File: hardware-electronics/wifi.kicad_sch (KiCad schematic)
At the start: 0 parts

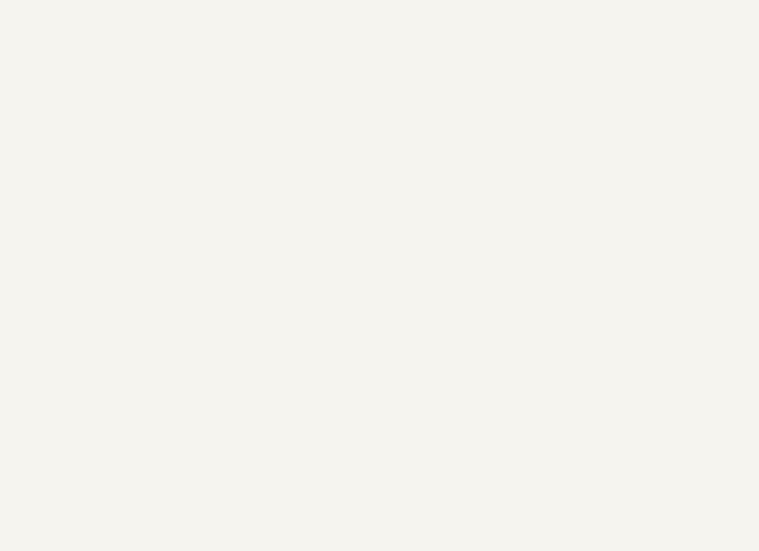
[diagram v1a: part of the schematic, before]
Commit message: [#9] SCH wifi add RTL8188FTV-VC-CG
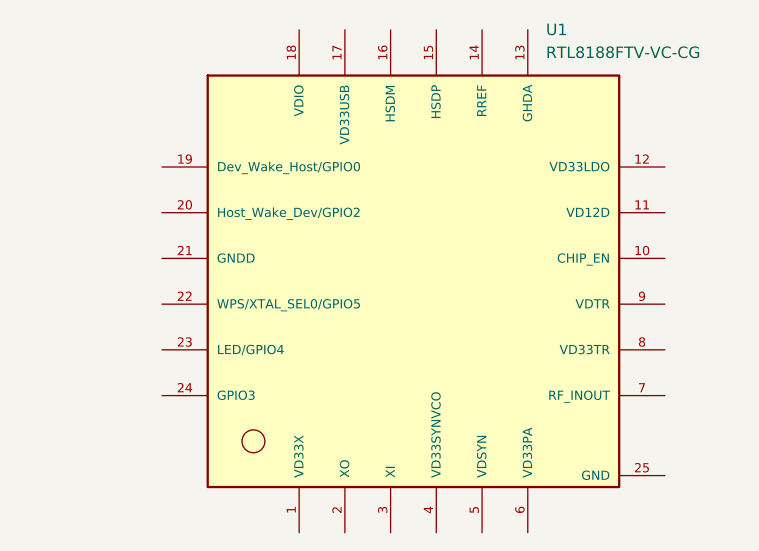
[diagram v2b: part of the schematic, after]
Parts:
- added U1: RTL8188FTV-VC-CG, RTL8188FTV-VC-CG, symbol M2SmartHomeSymbols:RTL8188FTV-VC-CG
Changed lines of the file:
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@@
+		)
+	)
+	(symbol
+		(lib_id "M2SmartHomeSymbols:RTL8188FTV-VC-CG")
+		(at 144.78 96.52 0)
+		(unit 1)
+		(exclude_from_sim no)
+		(in_bom yes)
+		(on_board yes)
+		(dnp no)
+		(fields_autoplaced yes)
+		(property "Reference" "U1"
+			(at 159.4994 68.58 0)
+			(effects
+				(font
+					(size 1.27 1.27)
+				)
+				(justify left)
+			)
+		)
+		(property "Value" "RTL8188FTV-VC-CG"
+			(at 159.4994 71.12 0)
+			(effects
+				(font
+					(size 1.27 1.27)
+				)
+				(justify left)
+			)
+		)
+		(property "Footprint" "RTL8188FTV-VC-CG"
+			(at 144.78 96.52 0)
+			(effects
+				(font
+					(size 1.27 1.27)
+				)
+				(justify bottom)
+				(hide yes)
+			)
+		)
+		(property "Datasheet" ""
+			(at 144.78 96.52 0)
+			(effects
+				(font
+					(size 1.27 1.27)
+				)
+				(hide yes)
+			)
+		)
+		(property "Description" ""
+			(at 144.78 96.52 0)
+			(effects
+				(font
+					(size 1.27 1.27)
+				)
+				(hide yes)
+			)
+		)
+		(property "MF" "Realtek"
+			(at 144.78 96.52 0)
+			(effects
+				(font
+					(size 1.27 1.27)
+				)
+				(justify bottom)
+				(hide yes)
+			)
+		)
+		(property "Description_1" ""
+			(at 144.78 96.52 0)
+			(effects
+				(font
+					(size 1.27 1.27)
+				)
+				(justify bottom)
+				(hide yes)
+			)
+		)
+		(property "Package" "QFN-24 Silicon Labs"
+			(at 144.78 96.52 0)
+			(effects
+				(font
+					(size 1.27 1.27)
+				)
+				(justify bottom)
+				(hide yes)
+			)
+		)
+		(property "Price" "None"
+			(at 144.78 96.52 0)
+			(effects
+				(font
+					(size 1.27 1.27)
+				)
+				(justify bottom)
+				(hide yes)
+			)
+		)
+		(property "Check_prices" ""
+			(at 144.78 96.52 0)
+			(effects
+				(font
+					(size 1.27 1.27)
+				)
+				(justify bottom)
+				(hide yes)
+			)
+		)
+		(property "PART_REV" "1.1"
+			(at 144.78 96.52 0)
+			(effects
+				(font
+					(size 1.27 1.27)
+				)
+				(justify bottom)
+				(hide yes)
+			)
+		)
+		(property "STANDARD" ""
+			(at 144.78 96.52 0)
+			(effects
+				(font
+					(size 1.27 1.27)
+				)
+				(justify bottom)
+				(hide yes)
+			)
+		)
+		(property "SnapEDA_Link" ""
+			(at 144.78 96.52 0)
+			(effects
+				(font
+					(size 1.27 1.27)
+				)
+				(justify bottom)
+				(hide yes)
+			)
+		)
+		(property "MP" "RTL8188FTV-VC-CG"
+			(at 144.78 96.52 0)
+			(effects
+				(font
+					(size 1.27 1.27)
+				)
+				(justify bottom)
+				(hide yes)
+			)
+		)
+		(property "Availability" "In Stock"
+			(at 144.78 96.52 0)
+			(effects
+				(font
+					(size 1.27 1.27)
+				)
+				(justify bottom)
+				(hide yes)
+			)
+		)
+		(property "MANUFACTURER" "Realtek"
+			(at 144.78 96.52 0)
+			(effects
+				(font
+					(size 1.27 1.27)
+				)
+				(justify bottom)
+				(hide yes)
+			)
+		)
+		(pin "18"
+		)
+		(pin "17"
+		)
+		(pin "16"
+		)
+		(pin "21"
+		)
+		(pin "19"
+		)
+		(pin "20"
+		)
+		(pin "2"
+		)
+		(pin "3"
+		)
+		(pin "25"
+		)
+		(pin "14"
+		)
+		(pin "13"
+		)
+		(pin "12"
+		)
+		(pin "9"
+		)
+		(pin "11"
+		)
+		(pin "24"
+		)
+		(pin "23"
+		)
+		(pin "10"
+		)
+		(pin "1"
+		)
+		(pin "4"
+		)
+		(pin "15"
+		)
+		(pin "22"
+		)
+		(pin "6"
+		)
+		(pin "5"
+		)
+		(pin "8"
+		)
+		(pin "7"
+		)
+		(instances
+			(project "M2SmartHome"
+				(path "/da663dec-9e91-4003-a791-431d460ad63c/7a341d5c-2113-408f-a1b4-1e4771333f4d"
+					(reference "U1")
+					(unit 1)
+				)
+			)
 		)
 	)

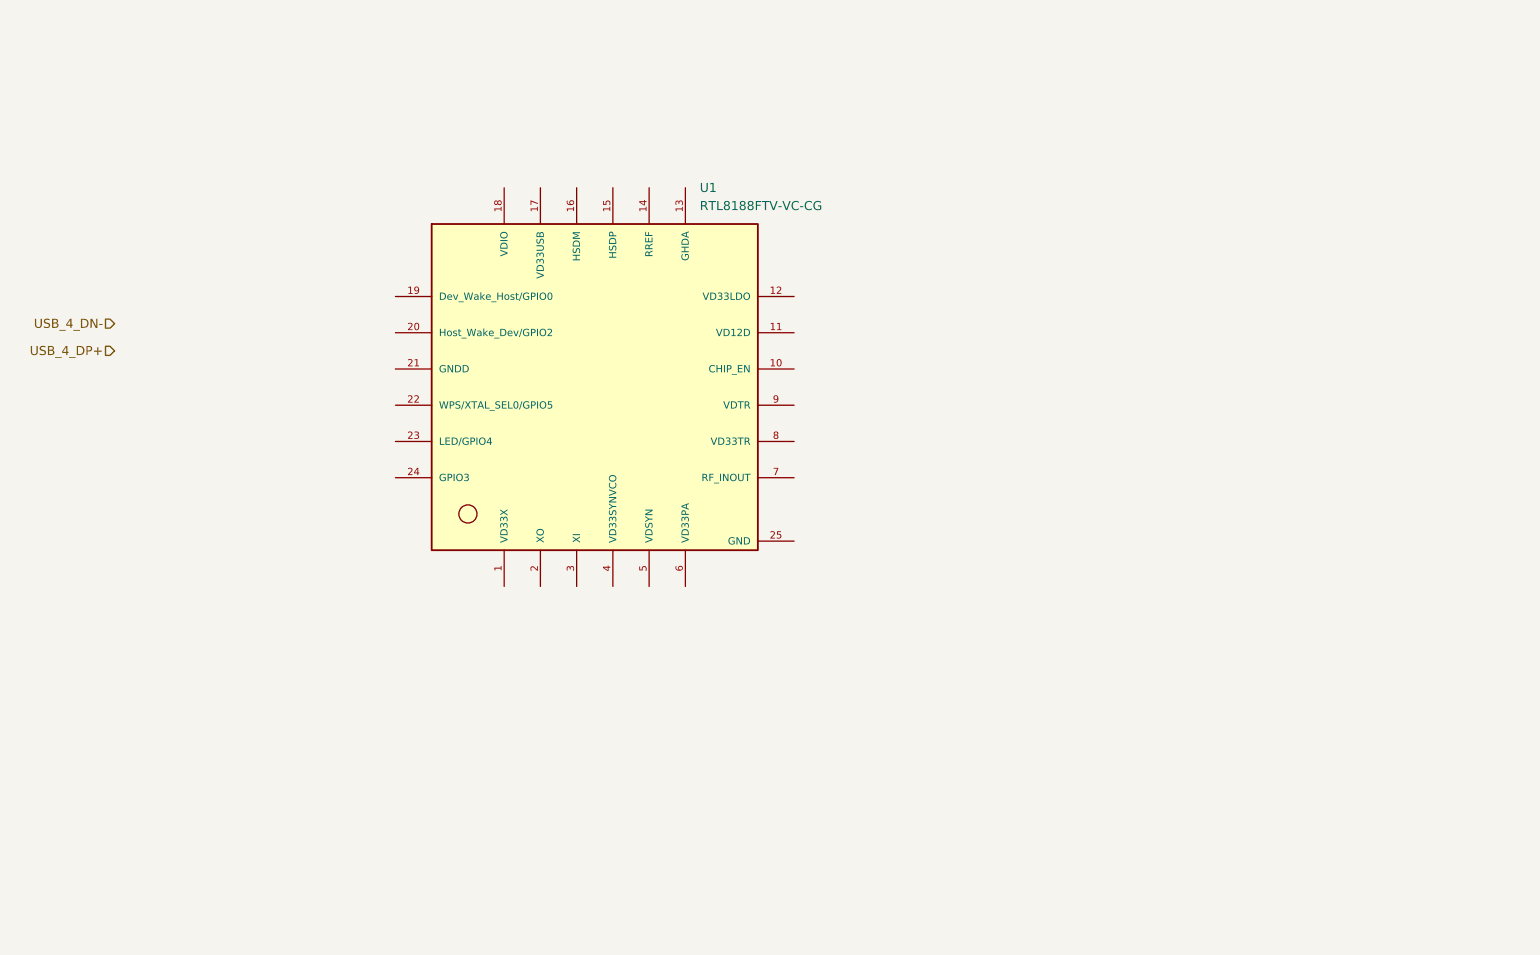
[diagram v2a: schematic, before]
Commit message: [#9] SCH wifi WIP RTL8188 connections
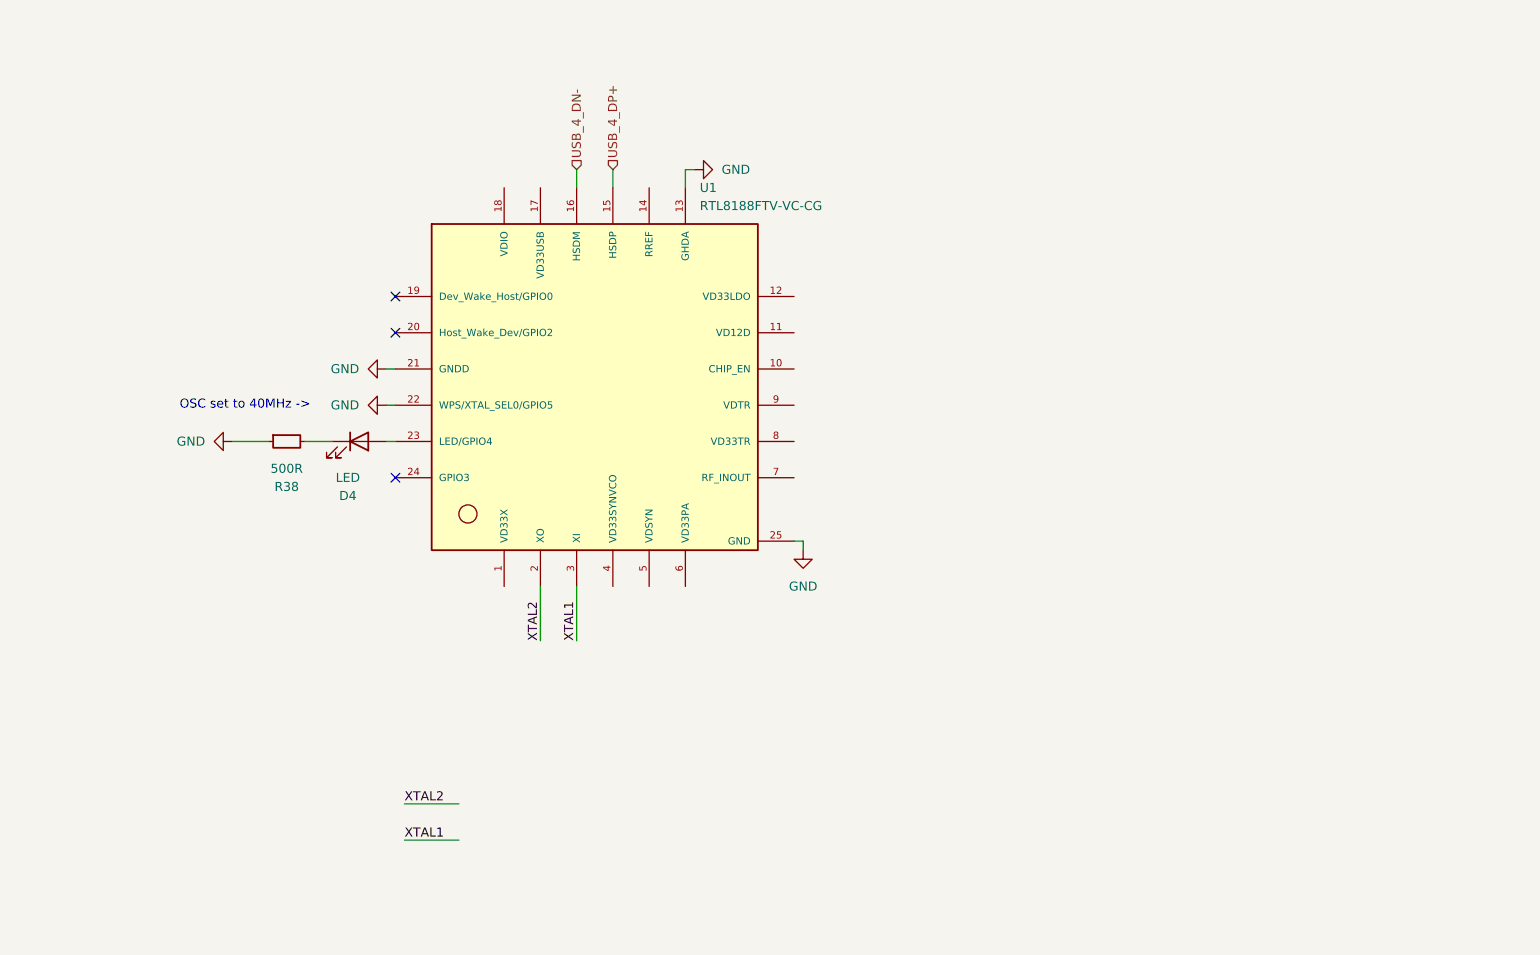
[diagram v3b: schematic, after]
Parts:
- added D4: LED, M2SmartHomeFootprints:LED_KPT-1608ZGC, symbol M2SmartHomeSymbols:KP-1608CGCK
- added R38: R_500R_0402, R_500R_0402:R_0402_1005Metric, symbol M2SmartHomeSymbols:R_500R_0402
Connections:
- net USB_4_DN-: now also U1.16 (HSDM)
- net USB_4_DP+: now also U1.15 (HSDP)
- net GND: now reaches U1.13 (GHDA)
- net GND: now also U1.21 (GNDD), U1.22 (WPS/XTAL_SEL0/GPIO5), U1.25 (GND), R38.1
- net XTAL2: now reaches U1.2 (XO)
- net at U1.23 (LED/GPIO4): now also D4.2 (A)
- net XTAL1: now reaches U1.3 (XI)
- new net: D4.1 (K), R38.2
- no-connect marks 0 -> 3
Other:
- note added: "OSC set to 40MHz ->"

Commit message: [#9] SCH wifi  RTL8188 power
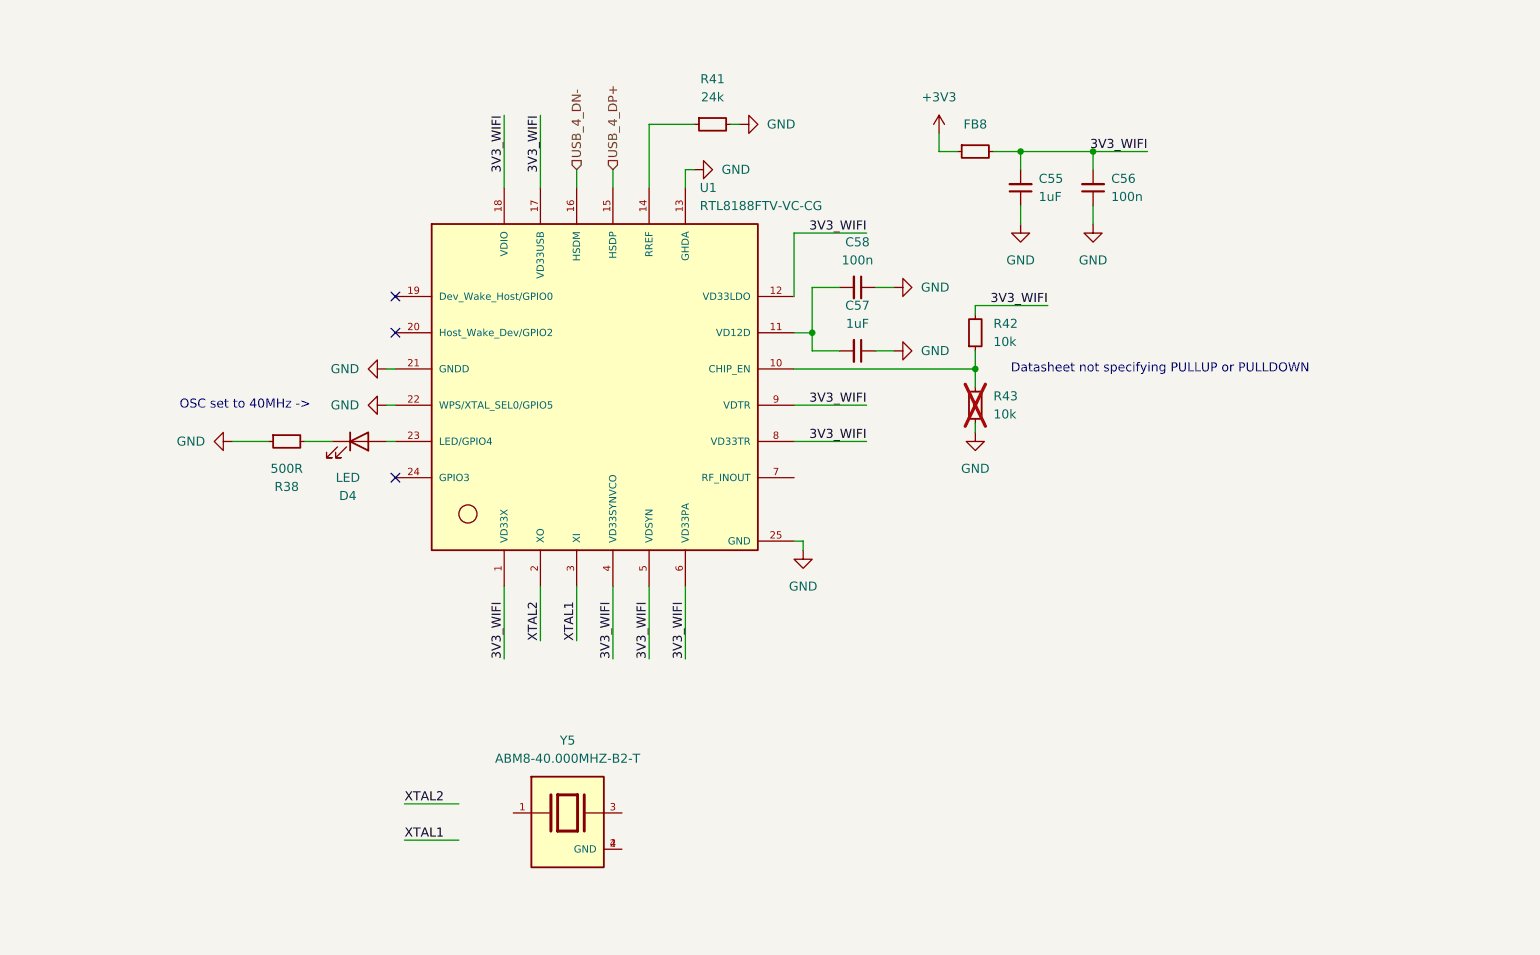
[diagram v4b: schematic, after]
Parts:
- added C55, C57: C_1uF_0402, C_1uF_0402:C_0402_1005Metric, symbol M2SmartHomeSymbols:C_1uF_0402
- added C56, C58: C_100n_0402, C_100n_0402:C_0402_1005Metric, symbol M2SmartHomeSymbols:C_100n_0402
- added FB8: FB_120R_0603, FB_120R_0603:FB_0603_1608Metric, symbol M2SmartHomeSymbols:FB_120R_0603
- added R41: R_24k_0402, R_24k_0402:R_0402_1005Metric, symbol M2SmartHomeSymbols:R_24k_0402
- added R42, R43: R_10k_0402, R_10k_0402:R_0402_1005Metric, symbol M2SmartHomeSymbols:R_10k_0402
- added Y5: ABM8-40.000MHZ-B2-T, ABM8-40.000MHZ-B2-T, symbol M2SmartHomeSymbols:ABM8-40.000MHZ-B2-T
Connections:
- net GND: now also C55.1, C56.1, C57.1, C58.1, R41.2, R43.1
- net 3V3_WIFI: now reaches U1.1 (VD33X)
- net 3V3_WIFI: now also U1.12 (VD33LDO), U1.17 (VD33USB), U1.18 (VDIO), U1.4 (VD33SYNVCO), U1.5 (VDSYN), U1.6 (VD33PA), U1.8 (VD33TR), U1.9 (VDTR), C55.2, C56.2, FB8.2, R42.2
- net at U1.10 (CHIP_EN): now also R42.1, R43.2
- net at U1.11 (VD12D): now also C57.2, C58.2
- net at U1.14 (RREF): now also R41.1
- new net: Y5.2 (GND), Y5.4 (GND)
- new net +3V3: FB8.1
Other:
- note added: "Datasheet not specifying PULLUP or PULLDOWN"

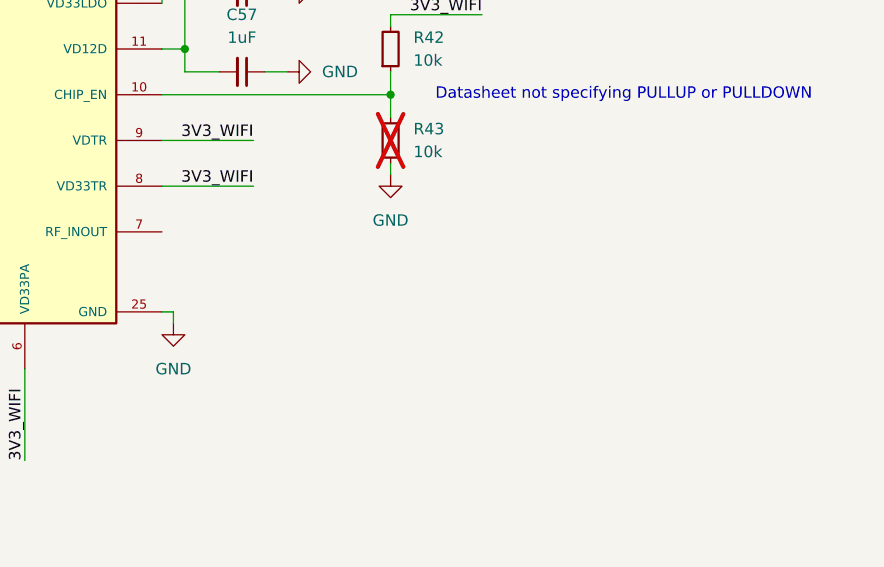
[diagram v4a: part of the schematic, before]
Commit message: [#9] SCH wifi add matching circuit copied from Thread radio
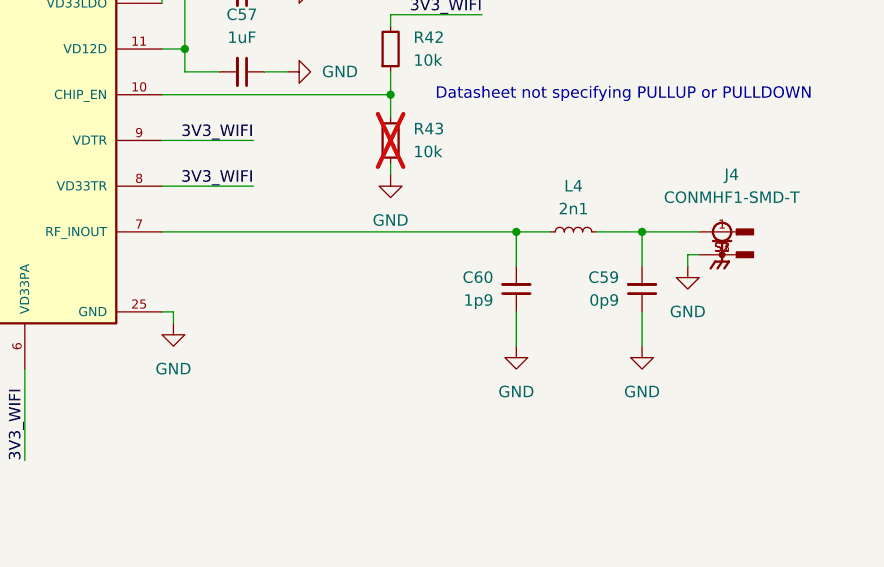
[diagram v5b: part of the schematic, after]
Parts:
- added C59: C_0p9_0201, C_0p9_0201:C_0201_0603Metric, symbol M2SmartHomeSymbols:C_0p9_0201
- added C60: C_1p9_0201, C_1p9_0201:C_0201_0603Metric, symbol M2SmartHomeSymbols:C_1p9_0201
- added J4: CONMHF1-SMD-T, CONMHF1-SMD-T:LINX_CONMHF1-SMD-T, symbol M2SmartHomeSymbols:CONMHF1-SMD-T
- added L4: L_2n1_0201, L_2n1_0201:L_0201_0603Metric, symbol M2SmartHomeSymbols:L_2n1_0201
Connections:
- net GND: now also C59.1, C60.1, J4.S1, J4.S2, J4.S3
- net at U1.7 (RF_INOUT): now also C60.2, L4.2
- new net: C59.2, J4.1, L4.1
